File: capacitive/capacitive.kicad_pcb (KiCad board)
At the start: 2 copper layers, 78 x 72 mm, 84 parts, among them J101 UL, J102 UART, J103 SWD, J104 TX_PADS, J105 RX_PAD, J106 POWER, J107 UR, J108 LL, J109 LR, Q101 RU1C002ZPTCL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

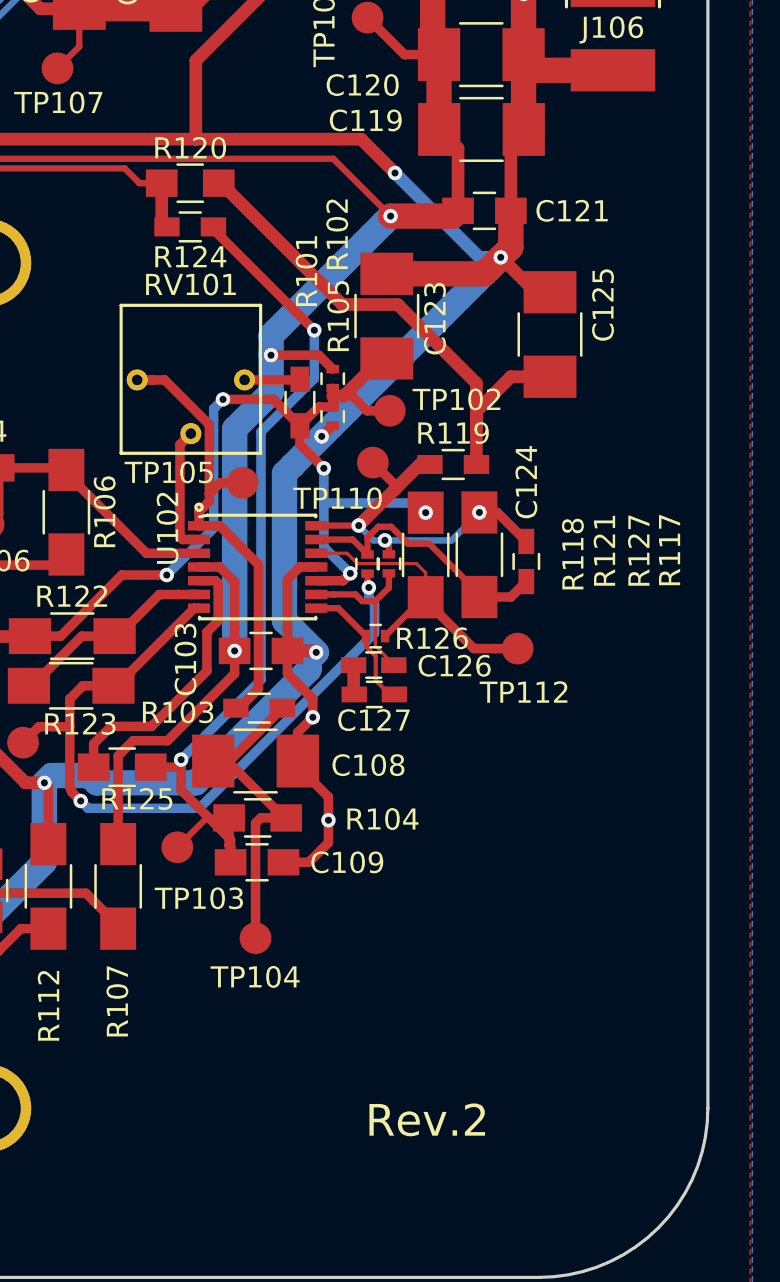
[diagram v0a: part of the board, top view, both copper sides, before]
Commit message: Convert over to Kicad 5, fix mistakes for next revision
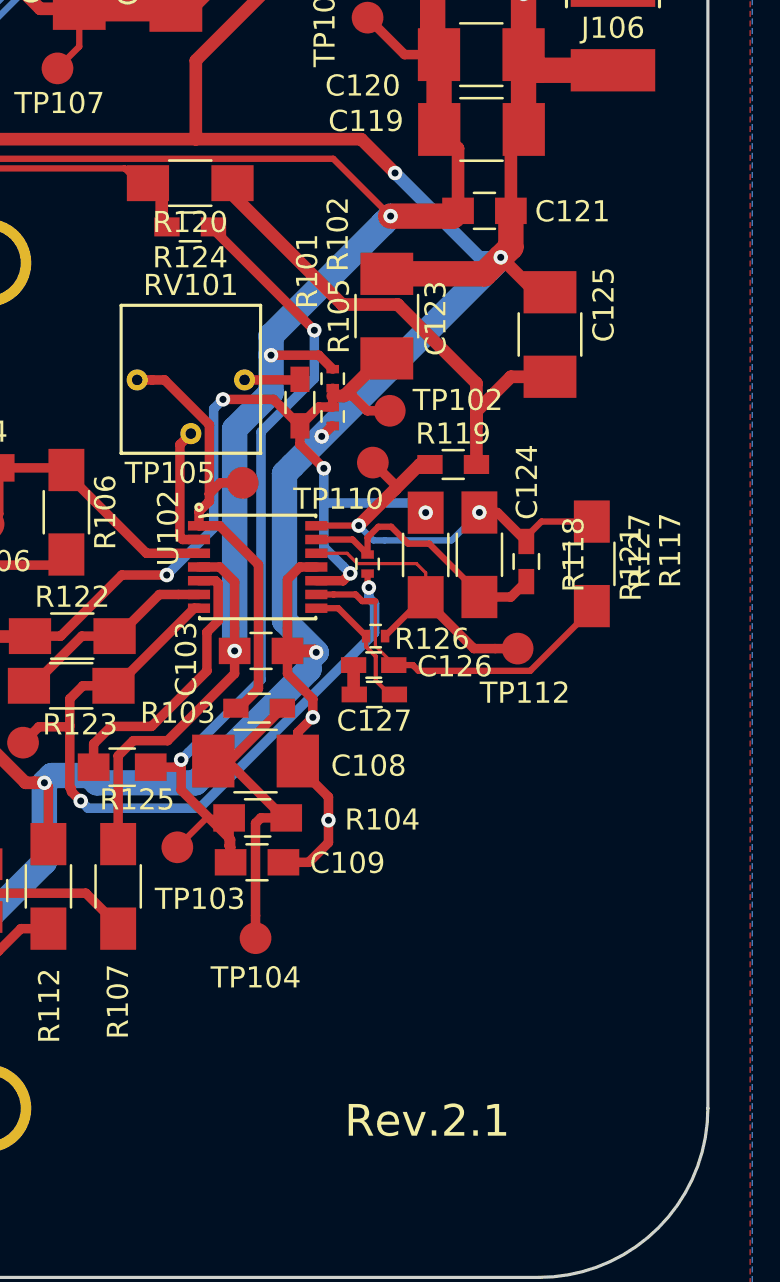
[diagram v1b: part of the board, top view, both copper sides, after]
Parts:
- R101: value 1k -> 100
- R120: footprint Resistors_SMD:R_0805_HandSoldering -> Resistors_SMD:R_1206_HandSoldering
- R121: value 10k 1% -> 100k 1%; footprint Resistors_SMD:R_0402 -> Resistors_SMD:R_1206_HandSoldering
- moved R121 9.60 mm to (143.5, 94.2)
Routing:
- net Net-(C126-Pad2): track 7.89 -> 17.1 mm
- net Net-(C124-Pad2): track 18.3 -> 21.2 mm, vias 3 -> 2
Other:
- board text added: "Rev.2.1"
- board text removed: "Rev.2"
